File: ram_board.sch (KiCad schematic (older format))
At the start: 17 parts, among them J1 Conn_02x20_Odd_Even, J2 Conn_02x05_Odd_Even, U1 IS61LV5128AL-10TLI, U2 SST39VF040-70-4C-NHE, U3 74LVC04A

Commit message: added switch, switch to 4 layer brd
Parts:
- added SW1: SW_DIP_x04, Button_Switch_SMD:SW_DIP_SPSTx04_Slide_KingTek_DSHP04TS_W7.62mm_P1.27mm, symbol Switch:SW_DIP_x04
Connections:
- net labels added: ROM_WE, SW0, SW1, SW2, SW3
- wire segments 139 -> 153
- no-connect marks 11 -> 6
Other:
- moved on the sheet: R2, U1, U2

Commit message: redesign
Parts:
- removed R4, R5, R6: 360R, Resistor_SMD:R_0603_1608Metric_Pad1.05x0.95mm_HandSolder, symbol Device:R_Small
- removed U3: 74LVC04A, Package_SO:TSSOP-14_4.4x5mm_P0.65mm, symbol ram_board-rescue:74LVC04ADR-74xx
- added R1: 360R, Resistor_SMD:R_0603_1608Metric_Pad1.05x0.95mm_HandSolder, symbol Device:R_Small
- added RN1: 1K, Resistor_SMD:R_Array_Convex_4x1206, symbol Device:R_Pack04
- added U4, U5: 74LVC2G04, Package_SO:TSOP-6_1.65x3.05mm_P0.95mm, symbol 74xGxx:74LVC2G04
- J1: value Conn_02x20_Odd_Even -> Bus
- J2: value Conn_02x05_Odd_Even -> PWR
- R2: value 10K -> 1K
- R3: Description Thick Film Resistors - SMD 360 ohm 1% -> Thick Film Resistors - SMD 10K 1% 1/10W; MPN CR0603-FX-3600ELF -> CR0603-FX-1002ELF
- SW1: value SW_DIP_x04 -> Config; footprint Button_Switch_SMD:SW_DIP_SPSTx04_Slide_KingTek_DSHP04TS_W7.62mm_P1.27mm -> Button_Switch_SMD:SW_DIP_SPSTx06_Slide_KingTek_DSHP06TS_W7.62mm_P1.27mm; symbol Switch:SW_DIP_x04 -> Switch:SW_DIP_x06
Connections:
- net labels added: SW1_0, SW1_1, SW1_2, SW1_3, SW1_4, SW1_5, VCC
- net labels removed: SW0, SW1, SW2, SW3
- wire segments 153 -> 165
- no-connect marks 6 -> 4
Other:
- note removed: "green"
- moved on the sheet: C4, C5, J1, J2

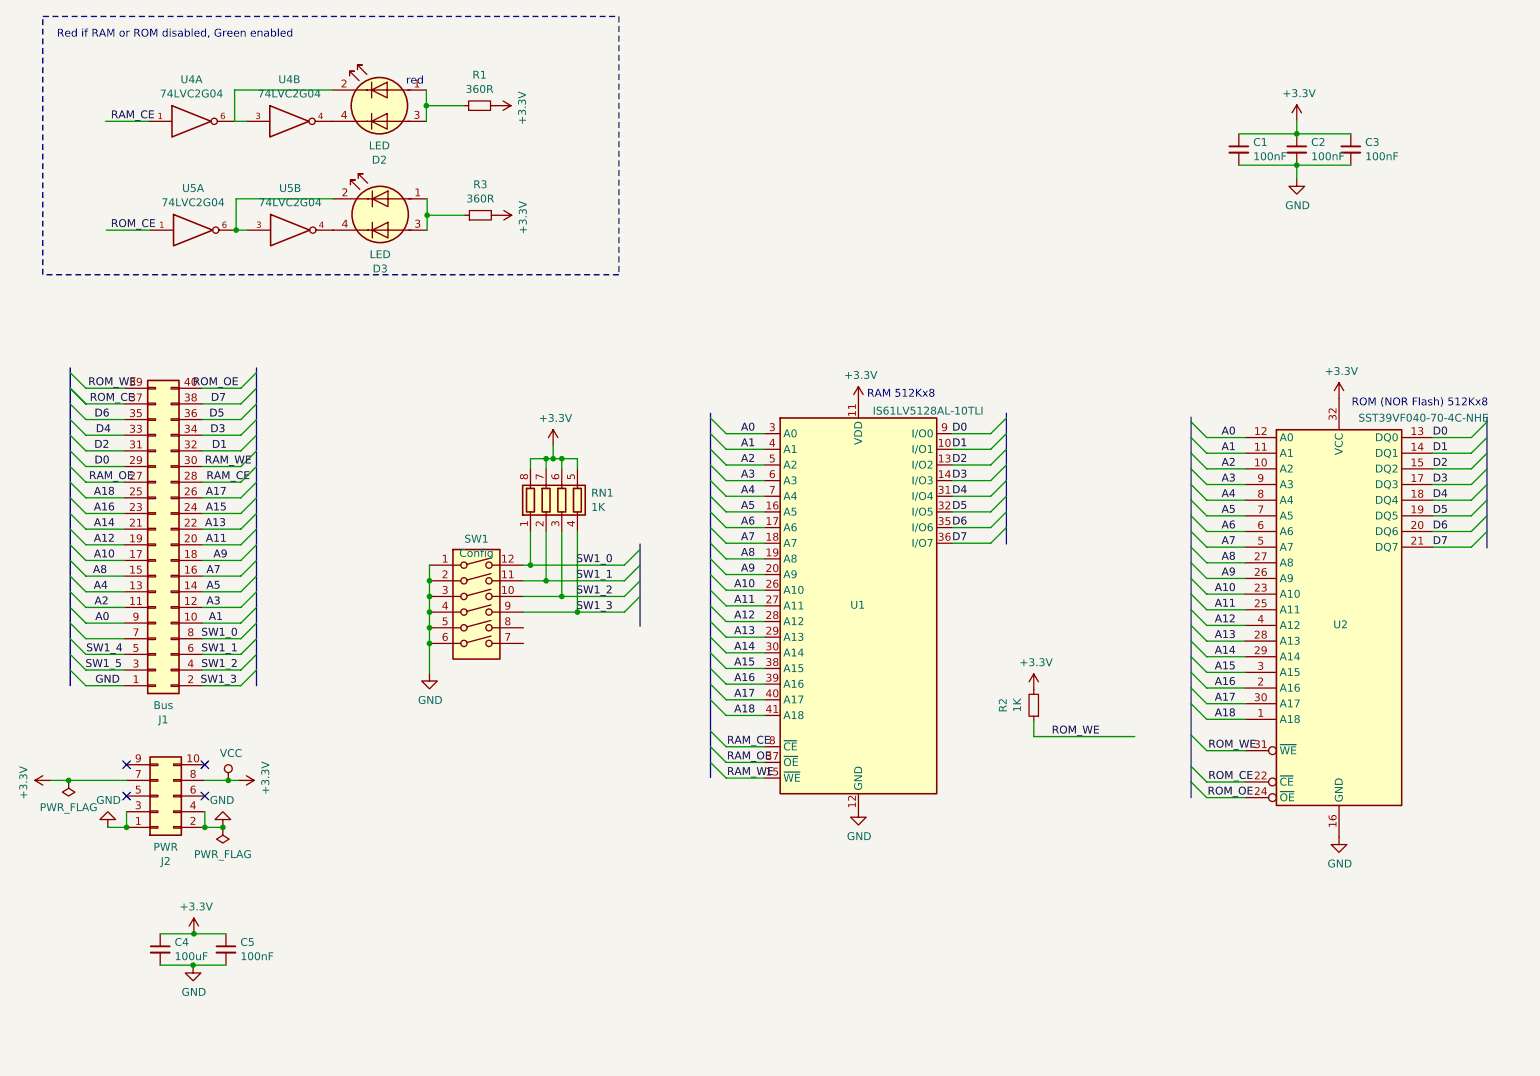
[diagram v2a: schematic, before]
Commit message: tri-state led driver
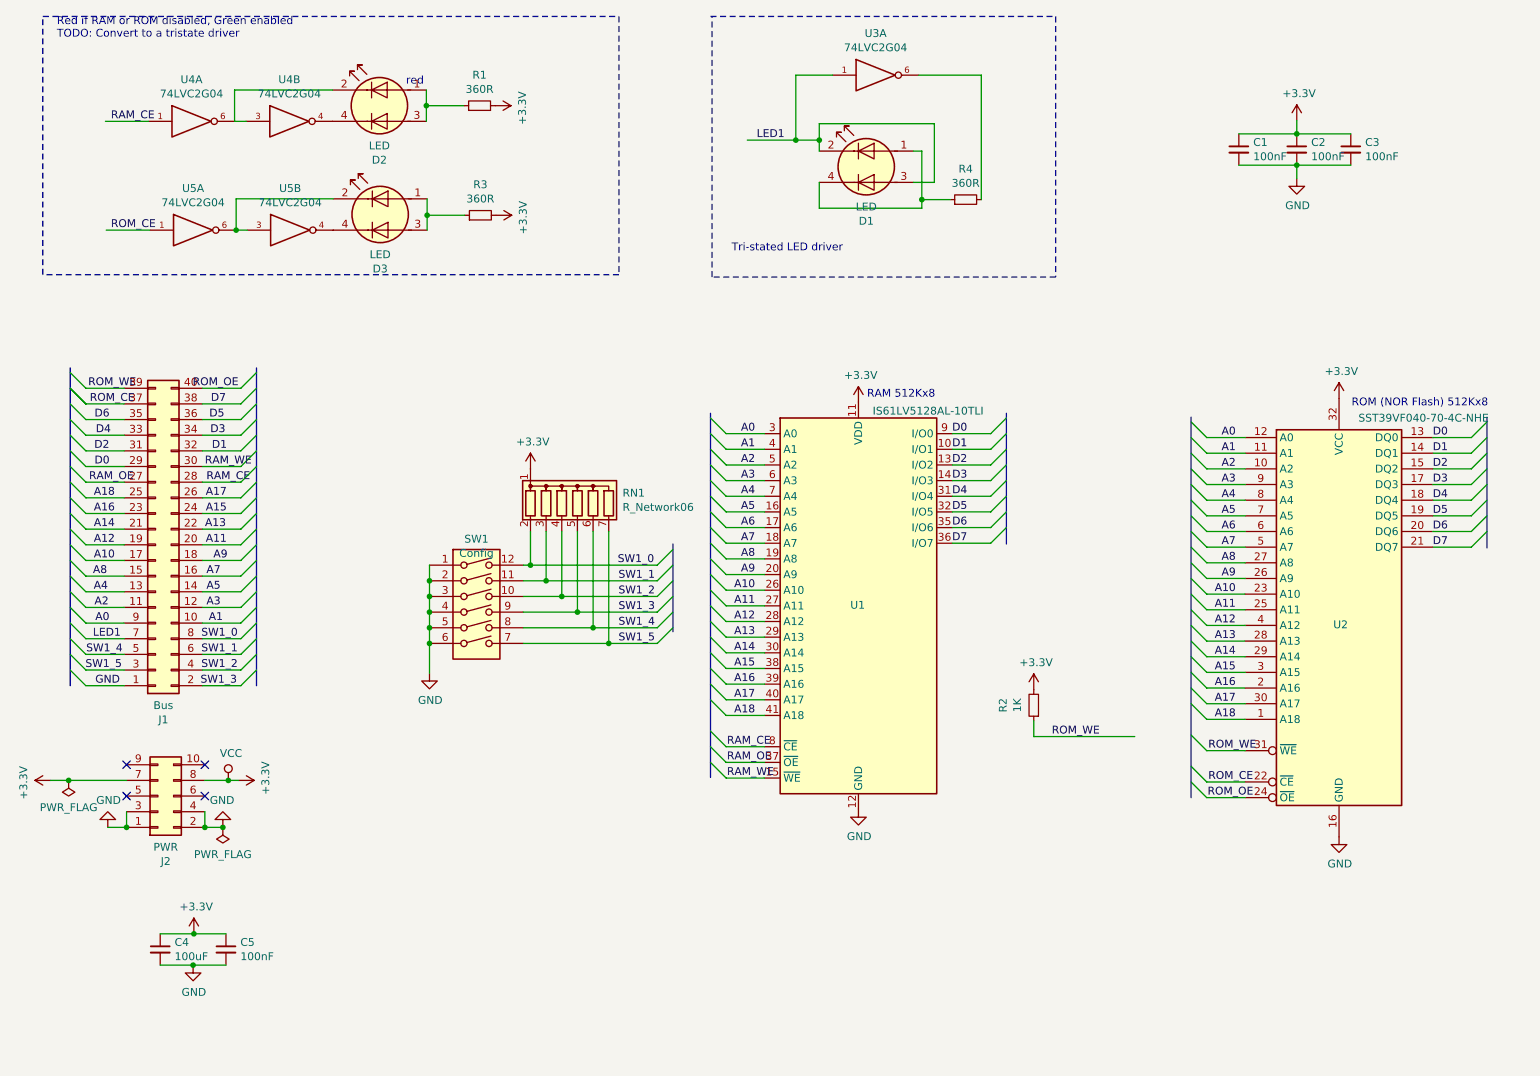
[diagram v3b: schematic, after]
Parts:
- removed RN1: 1K, Resistor_SMD:R_Array_Convex_4x1206, symbol Device:R_Pack04
- added D1: LED, LED_SMD:LED_2C_0603_1608Metric_Pad1.05x0.95mm_HandSolder, symbol Device:LED_Dual_ACAC
- added R4: 360R, Resistor_SMD:R_0603_1608Metric_Pad1.05x0.95mm_HandSolder, symbol Device:R_Small
- added RN1: R_Network06, Resistor_SMD:R_Array_Convex_8x0602, symbol Device:R_Network06
- added U3: 74LVC2G04, Package_SO:TSOP-6_1.65x3.05mm_P0.95mm, symbol 74xGxx:74LVC2G04
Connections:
- net labels added: LED1
- wire segments 165 -> 179
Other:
- note added: "Red if RAM or ROM disabled, Green enabled\nTODO: Convert to a tristate driver"
- note added: "Tri-stated LED driver"
- note removed: "Red if RAM or ROM disabled, Green enabled"
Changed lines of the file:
@@
 	1435 1335 1160 1335
 Text Notes 850  810  0    50   ~ 0
-Red if RAM or ROM disabled, Green enabled
+Red if RAM or ROM disabled, Green enabled\nTODO: Convert to a tristate driver
 Text Notes 6025 3110 0    50   ~ 0
 RAM 512Kx8
@@
 	1    0    0    -1
 $EndComp
-Text Label 4400 4470 2    50   ~ 0
+Text Label 4670 4470 2    50   ~ 0
 SW1_3
-Text Label 4400 4370 2    50   ~ 0
+Text Label 4670 4370 2    50   ~ 0
 SW1_2
-Text Label 4400 4270 2    50   ~ 0
+Text Label 4670 4270 2    50   ~ 0
 SW1_1
-Text Label 4400 4170 2    50   ~ 0
+Text Label 4665 4170 2    50   ~ 0
 SW1_0
-Entry Wire Line
-	4475 4470 4575 4370
-Entry Wire Line
-	4475 4370 4575 4270
-Entry Wire Line
-	4475 4270 4575 4170
-Entry Wire Line
-	4475 4170 4575 4070
 $Comp
 L power:GND #PWR02
@@
 	1    0    0    -1
 $EndComp
-Wire Wire Line
-	3875 3555 3875 3490
-Wire Wire Line
-	4175 3490 4175 3555
-Wire Wire Line
-	3975 3555 3975 3490
-Wire Wire Line
-	3875 3490 3975 3490
-Connection ~ 3975 3490
-Wire Wire Line
-	3975 3490 4020 3490
-Wire Wire Line
-	4075 3555 4075 3490
-Connection ~ 4075 3490
-Wire Wire Line
-	4075 3490 4175 3490
 $Comp
 L power:+3.3V #PWR01
 U 1 1 5D3D2CF9
-P 4020 3405
-F 0 "#PWR01" H 4020 3255 50  0001 C CNN
-F 1 "+3.3V" H 4035 3578 50  0000 C CNN
-F 2 "" H 4020 3405 50  0001 C CNN
-F 3 "" H 4020 3405 50  0001 C CNN
-	1    4020 3405
-	1    0    0    -1
-$EndComp
-Wire Wire Line
-	4020 3405 4020 3490
-Connection ~ 4020 3490
-Wire Wire Line
-	4020 3490 4075 3490
-$Comp
-L Device:R_Pack04 RN1
-U 1 1 5D40BED1
-P 4075 3755
-F 0 "RN1" H 4263 3801 50  0000 L CNN
-F 1 "1K" H 4263 3710 50  0000 L CNN
-F 2 "Resistor_SMD:R_Array_Convex_4x1206" V 4350 3755 50  0001 C CNN
-F 3 "~" H 4075 3755 50  0001 C CNN
-	1    4075 3755
-	1    0    0    -1
-$EndComp
-Wire Wire Line
-	3830 4270 3975 4270
+P 3875 3555
+F 0 "#PWR01" H 3875 3405 50  0001 C CNN
+F 1 "+3.3V" H 3890 3728 50  0000 C CNN
+F 2 "" H 3875 3555 50  0001 C CNN
+F 3 "" H 3875 3555 50  0001 C CNN
+	1    3875 3555
+	1    0    0    -1
+$EndComp
 Wire Wire Line
 	3830 4370 4075 4370
@@
 Wire Wire Line
 	3875 3955 3875 4170
-Connection ~ 3875 4170
-Wire Wire Line
-	3875 4170 4475 4170
 Wire Wire Line
 	3975 3955 3975 4270
-Connection ~ 3975 4270
-Wire Wire Line
-	3975 4270 4475 4270
 Wire Wire Line
 	4075 3955 4075 4370
-Connection ~ 4075 4370
-Wire Wire Line
-	4075 4370 4475 4370
 Wire Wire Line
 	4175 3955 4175 4470
-Connection ~ 4175 4470
-Wire Wire Line
-	4175 4470 4475 4470
 Wire Wire Line
 	1295 5845 1295 5745
@@
 Wire Wire Line
 	3230 4670 3230 4860
+Text Label 4670 4670 2    50   ~ 0
+SW1_5
+Text Label 4670 4570 2    50   ~ 0
+SW1_4
+Wire Wire Line
+	4275 3955 4275 4570
+Wire Wire Line
+	4375 3955 4375 4670
+$Comp
+L Device:R_Network06 RN1
+U 1 1 5D2A07A4
+P 4175 3755
+F 0 "RN1" H 4463 3801 50  0000 L CNN
+F 1 "R_Network06" H 4463 3710 50  0000 L CNN
+F 2 "Resistor_SMD:R_Array_Convex_8x0602" V 4550 3755 50  0001 C CNN
+F 3 "http://www.vishay.com/docs/31509/csc.pdf" H 4175 3755 50  0001 C CNN
+	1    4175 3755
+	1    0    0    -1
+$EndComp
+Entry Wire Line
+	4685 4570 4785 4470
+Entry Wire Line
+	4685 4670 4785 4570
+Wire Wire Line
+	3830 4670 4375 4670
+Wire Wire Line
+	3830 4570 4275 4570
+Wire Wire Line
+	4175 4470 4685 4470
+Wire Wire Line
+	4075 4370 4685 4370
+Entry Wire Line
+	4685 4170 4785 4070
+Entry Wire Line
+	4685 4270 4785 4170
+Entry Wire Line
+	4685 4370 4785 4270
+Entry Wire Line
+	4685 4470 4785 4370
+Wire Wire Line
+	3875 4170 4685 4170
+Connection ~ 3875 4170
+Wire Wire Line
+	3830 4270 3975 4270
+Wire Wire Line
+	3975 4270 4685 4270
+Connection ~ 3975 4270
+Connection ~ 4075 4370
+Connection ~ 4175 4470
+Connection ~ 4275 4570
+Wire Wire Line
+	4275 4570 4685 4570
+Connection ~ 4375 4670
+Wire Wire Line
+	4375 4670 4685 4670
+$Comp
+L Device:LED_Dual_ACAC D1
+U 1 1 5D40BBB0
+P 6020 1625
+F 0 "D1" H 6020 1278 50  0000 C CNN
+F 1 "LED" H 6020 1369 50  0000 C CNN
+F 2 "LED_SMD:LED_2C_0603_1608Metric_Pad1.05x0.95mm_HandSolder" H 6050 1625 50  0001 C CNN
+F 3 "https://www.mouser.com/datasheet/2/348/sml-d22-e-1508165.pdf" H 6050 1625 50  0001 C CNN
+F 4 "Standard LEDs - SMD Red/YelGrn 620/570nm 16/10mcd 65/67mW 5mA" H 6020 1625 50  0001 C CNN "Description"
+F 5 "SML-D22MUWT86" H 6020 1625 50  0001 C CNN "MPN"
+F 6 "ROHM Semiconductor" H 6020 1625 50  0001 C CNN "Manufacturer"
+	1    6020 1625
+	-1   0    0    -1
+$EndComp
+$Comp
+L Device:R_Small R4
+U 1 1 5D40BBBA
+P 6655 1835
+F 0 "R4" V 6851 1835 50  0000 C CNN
+F 1 "360R" V 6760 1835 50  0000 C CNN
+F 2 "Resistor_SMD:R_0603_1608Metric_Pad1.05x0.95mm_HandSolder" H 6655 1835 50  0001 C CNN
+F 3 "https://www.mouser.com/datasheet/2/54/hpreztr-777398.pdf" H 6655 1835 50  0001 C CNN
+F 4 "Thick Film Resistors - SMD 10K 1% 1/10W" H 6655 1835 50  0001 C CNN "Description"
+F 5 "CR0603-FX-1002ELF" H 6655 1835 50  0001 C CNN "MPN"
+F 6 "Bourns" H 6655 1835 50  0001 C CNN "Manufacturer"
+	1    6655 1835
+	0    -1   -1   0
+$EndComp
+Wire Wire Line
+	6375 1835 6555 1835
+Wire Wire Line
+	5720 1525 5720 1455
+Wire Wire Line
+	5720 1350 6455 1350
+Wire Wire Line
+	6455 1350 6455 1725
+Wire Wire Line
+	6455 1725 6320 1725
+Wire Wire Line
+	6320 1525 6375 1525
+Wire Wire Line
+	6375 1525 6375 1835
+Wire Wire Line
+	6375 1890 5720 1890
+Wire Wire Line
+	5720 1890 5720 1725
+Connection ~ 6375 1835
+Wire Wire Line
+	6375 1835 6375 1890
+$Comp
+L 74xGxx:74LVC2G04 U3
+U 1 1 5D486330
+P 6105 1040
+F 0 "U3" H 6080 1307 50  0000 C CNN
+F 1 "74LVC2G04" H 6080 1216 50  0000 C CNN
+F 2 "Package_SO:TSOP-6_1.65x3.05mm_P0.95mm" H 6105 1040 50  0001 C CNN
+F 3 "http://www.ti.com/lit/sg/scyt129e/scyt129e.pdf" H 6105 1040 50  0001 C CNN
+	1    6105 1040
+	1    0    0    -1
+$EndComp
+Wire Wire Line
+	6755 1040 6355 1040
+Wire Wire Line
+	5805 1040 5570 1040
+Wire Wire Line
+	5570 1040 5570 1455
+Wire Wire Line
+	5570 1455 5720 1455
+Connection ~ 5720 1455
+Wire Wire Line
+	5720 1455 5720 1350
+Wire Wire Line
+	5570 1455 5260 1455
+Connection ~ 5570 1455
+Wire Wire Line
+	6755 1040 6755 1835
+Text Label 1080 4640 0    50   ~ 0
+LED1
+Text Label 5320 1455 0    50   ~ 0
+LED1
+Wire Notes Line
+	5025 665  7230 665
+Wire Notes Line
+	7230 665  7230 2330
+Wire Notes Line
+	7230 2330 5035 2330
+Wire Notes Line
+	5035 2330 5035 665
 Wire Bus Line
 	6915 3200 6915 4035
@@
 	9985 3225 9985 4060
 Wire Bus Line
-	4575 4035 4575 4560
+	4785 4035 4785 4595
 Wire Bus Line
 	935  2910 935  4940
@@
 Wire Bus Line
 	8095 3225 8095 5655
+Text Notes 5160 2175 0    50   ~ 0
+Tri-stated LED driver
 $EndSCHEMATC

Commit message: switched to discrete resistors,
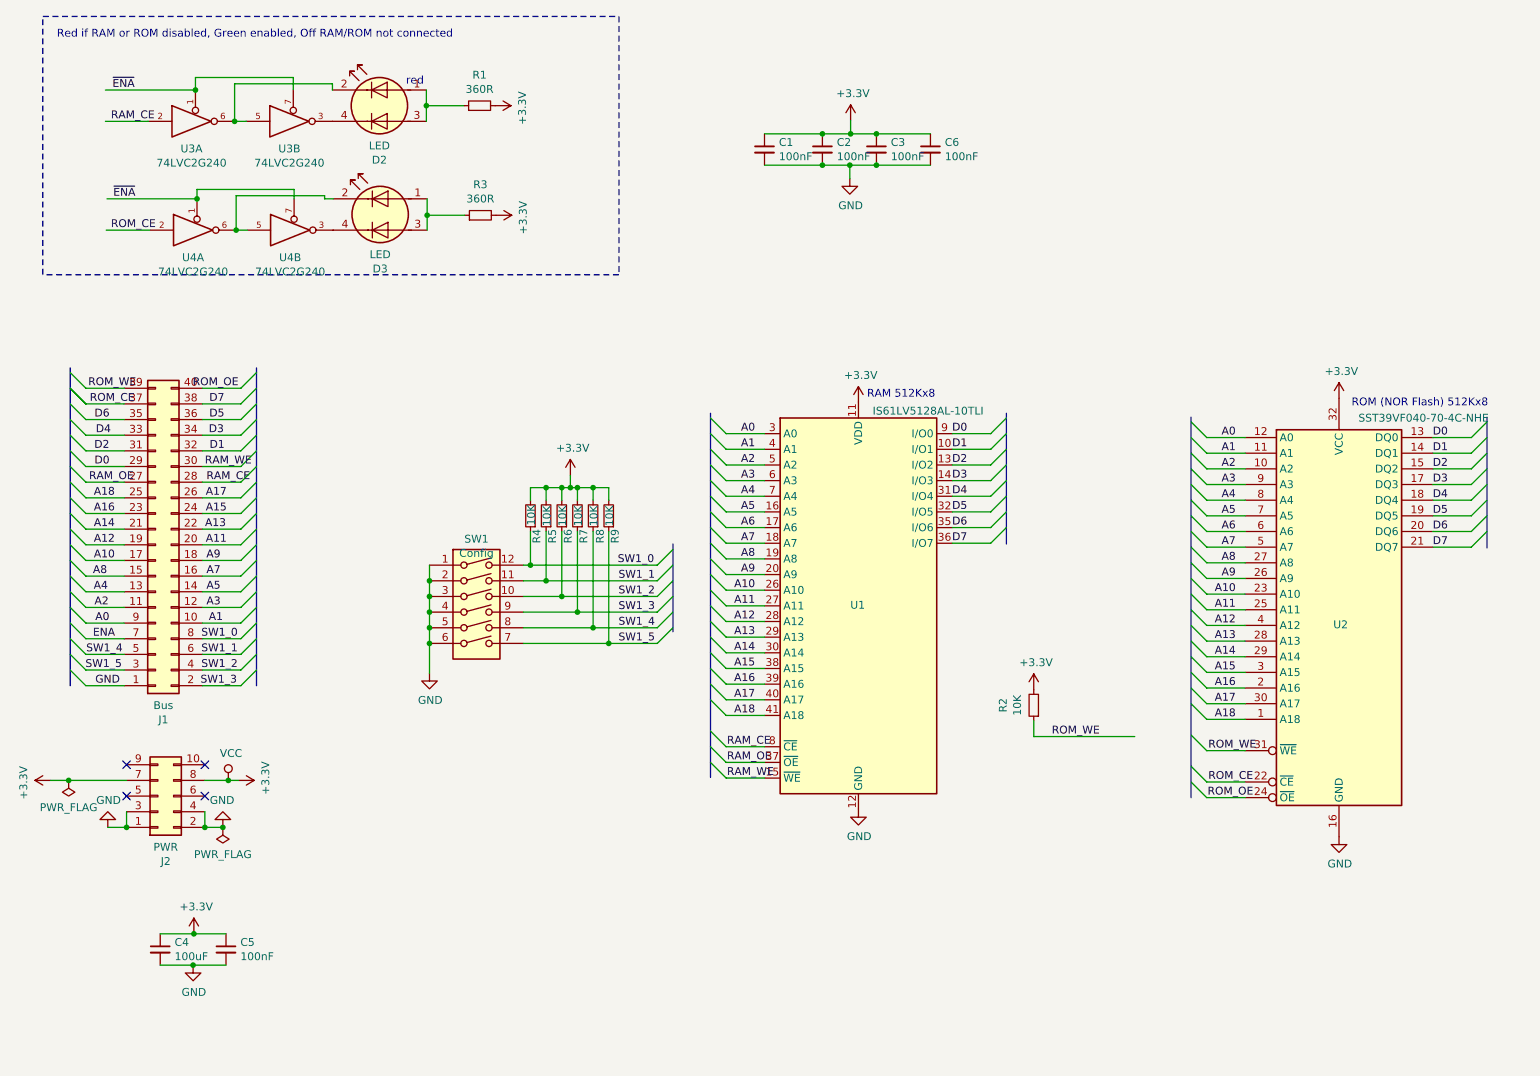
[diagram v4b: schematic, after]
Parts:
- removed D1: LED, LED_SMD:LED_2C_0603_1608Metric_Pad1.05x0.95mm_HandSolder, symbol Device:LED_Dual_ACAC
- removed RN1: R_Network06, Resistor_SMD:R_Array_Convex_8x0602, symbol Device:R_Network06
- removed U3, U4, U5: 74LVC2G04, Package_SO:TSOP-6_1.65x3.05mm_P0.95mm, symbol 74xGxx:74LVC2G04
- added C6: 100nF, Capacitor_SMD:C_0603_1608Metric_Pad1.05x0.95mm_HandSolder, symbol Device:C_Small
- added R5, R6, R7, R8, R9: 10K, Resistor_SMD:R_0603_1608Metric_Pad1.05x0.95mm_HandSolder, symbol Device:R_Small
- added U3, U4: 74LVC2G240, Package_SO:TSSOP-8_3x3mm_P0.65mm, symbol 74xGxx:74LVC2G240
- R2: value 1K -> 10K
- R4: value 360R -> 10K
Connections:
- net labels added: ENA, ~ENA
- net labels removed: LED1
- wire segments 179 -> 190
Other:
- note added: "Red if RAM or ROM disabled, Green enabled, Off RAM/ROM not connected\n"
- note removed: "Red if RAM or ROM disabled, Green enabled\nTODO: Convert to a tristate driver"
- note removed: "Tri-stated LED driver"
- moved on the sheet: C1, C2, C3

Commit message: simplified pins, finished routing
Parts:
- removed R4: 10K, Resistor_SMD:R_0603_1608Metric_Pad1.05x0.95mm_HandSolder, symbol Device:R_Small
- added C7: 100nF, Capacitor_SMD:C_0603_1608Metric_Pad1.05x0.95mm_HandSolder, symbol Device:C_Small
- added U5: 74LVC2G32, Package_SO:TSSOP-8_3x3mm_P0.65mm, symbol 74xGxx:74LVC2G32
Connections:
- net labels added: ~RAM, ~RD, ~ROM, ~WR
- net labels removed: ENA, RAM_OE, RAM_WE, ROM_OE, ROM_WE
- wire segments 190 -> 192
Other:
- moved on the sheet: J2, U2

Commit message: fixed up LED's and muxed signals
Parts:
- removed C6, C7: 100nF, Capacitor_SMD:C_0603_1608Metric_Pad1.05x0.95mm_HandSolder, symbol Device:C_Small
- removed D3: LED, LED_SMD:LED_2C_0603_1608Metric_Pad1.05x0.95mm_HandSolder, symbol Device:LED_Dual_ACAC
- removed U4: 74LVC2G240, Package_SO:TSSOP-8_3x3mm_P0.65mm, symbol 74xGxx:74LVC2G240
- removed U5: 74LVC2G32, Package_SO:TSSOP-8_3x3mm_P0.65mm, symbol 74xGxx:74LVC2G32
- added D1: LED, LED_SMD:LED_2C_0603_1608Metric_Pad1.05x0.95mm_HandSolder, symbol Device:LED_Dual_ACAC
- added R4: 360R, Resistor_SMD:R_0603_1608Metric_Pad1.05x0.95mm_HandSolder, symbol Device:R_Small
- C1, C2, C3: Description Multilayer Ceramic Capacitors MLCC - SMD/SMT .1uF 50V X7R 5% -> (none); MPN CC0603JRX7R9BB104 -> (none); Manufacturer Yageo -> (none)
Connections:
- net labels added: LED_G, LED_R
- net labels removed: RAM_CE, ROM_CE
- wire segments 192 -> 176
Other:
- note removed: "Red if RAM or ROM disabled, Green enabled, Off RAM/ROM not connected\n"
- moved on the sheet: D2, R1, R2, R5, R6, R7, R8, R9, SW1, U3A, U3B
